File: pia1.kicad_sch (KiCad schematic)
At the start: 33 parts, among them IC20 MC14529B, IC24 74LS244N, IC25 LM393P, IC26 MC6821

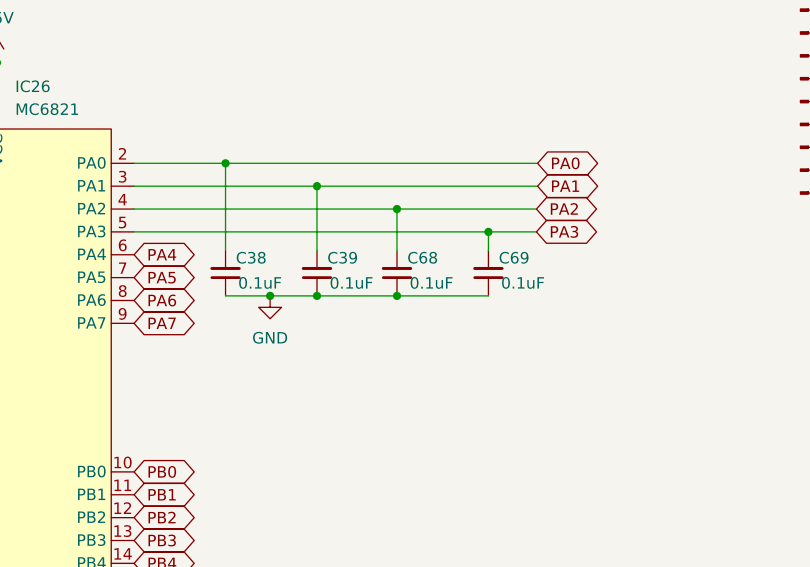
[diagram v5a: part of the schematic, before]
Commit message: update capacitor values for joystick button input
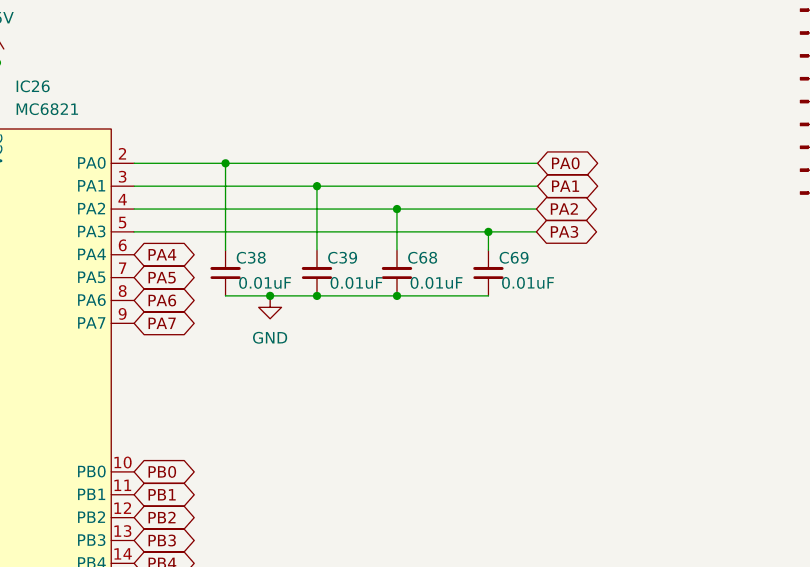
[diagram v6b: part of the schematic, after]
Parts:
- C38, C39, C68, C69: value 0.1uF -> 0.01uF
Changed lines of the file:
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@@
       (effects (font (size 1.27 1.27)) (justify right))
     )
-    (property "Value" "0.1uF" (id 1) (at 114.935 72.009 0)
+    (property "Value" "0.01uF" (id 1) (at 114.935 72.009 0)
       (effects (font (size 1.27 1.27)) (justify right))
     )
@@
       (effects (font (size 1.27 1.27)) (justify right))
     )
-    (property "Value" "0.1uF" (id 1) (at 85.725 72.009 0)
+    (property "Value" "0.01uF" (id 1) (at 85.725 72.009 0)
       (effects (font (size 1.27 1.27)) (justify right))
     )
@@
       (effects (font (size 1.27 1.27)) (justify right))
     )
-    (property "Value" "0.1uF" (id 1) (at 104.775 72.009 0)
+    (property "Value" "0.01uF" (id 1) (at 104.775 72.009 0)
       (effects (font (size 1.27 1.27)) (justify right))
     )
@@
       (effects (font (size 1.27 1.27)) (justify right))
     )
-    (property "Value" "0.1uF" (id 1) (at 95.885 72.009 0)
-      (effects (font (size 1.27 1.27)) (justify right))
-    )
+    (property "Value" "0.01uF" (id 1) (at 95.885 72.009 0)
+      (effects (font (size 1.27 1.27)) (justify right))
+    )

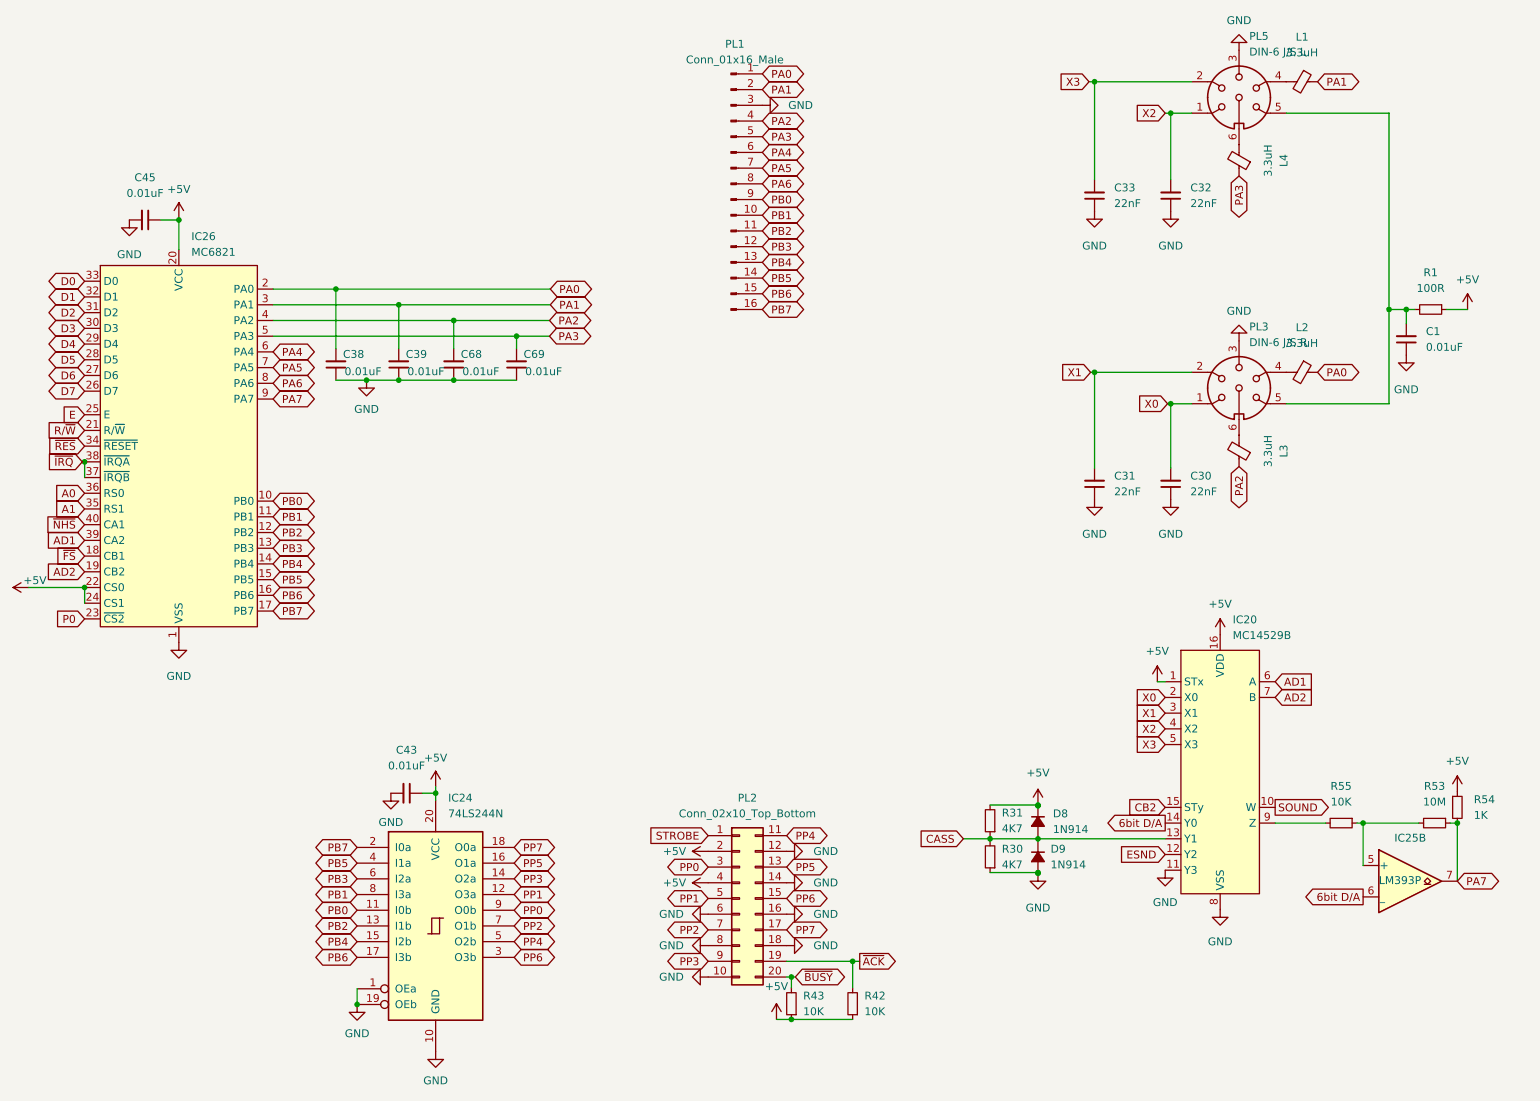
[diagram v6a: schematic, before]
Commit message: add trace labels for joysticks
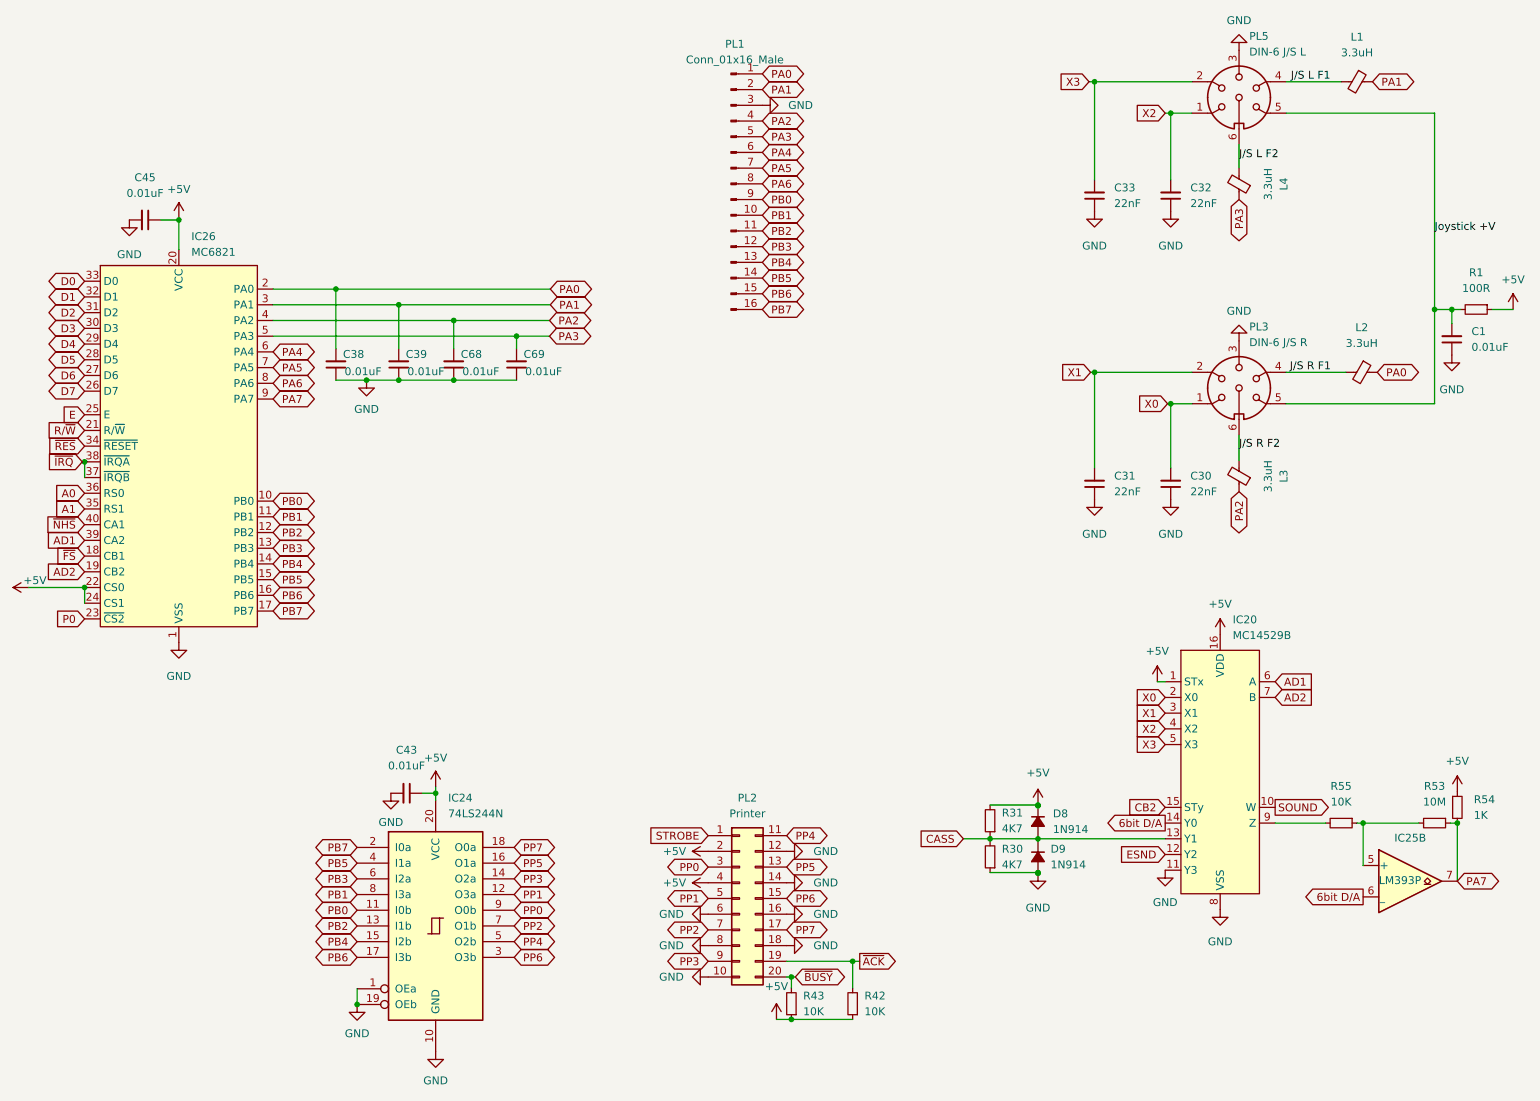
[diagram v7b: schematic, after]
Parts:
- PL2: value Conn_02x10_Top_Bottom -> Printer
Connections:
- net Joystick +V: now reaches C1.2, PL3.5, PL5.5, R1.2
- net J/S L F1: now reaches L1.2, PL5.4
- net J/S L F2: now reaches L4.2, PL5.6
- net J/S R F1: now reaches L2.2, PL3.4
- net J/S R F2: now reaches L3.2, PL3.6
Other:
- moved on the sheet: C1, L1, L2, L3, L4, R1
